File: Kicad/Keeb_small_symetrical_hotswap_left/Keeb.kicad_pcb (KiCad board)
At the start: 2 copper layers, 96.3 x 99.3 mm, 28 parts, among them J1 TYPE-C-31-M-12, SW1 CherryMX, SW10 CherryMX, SW11 CherryMX, SW13 CherryMX, SW14 CherryMX, SW15 CherryMX, SW16 CherryMX, SW17 CherryMX, SW18 CherryMX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

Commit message: added encoder
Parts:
- added U2: KY-040, KY-040:KY-040-PORT, F.Cu at (110.7, 38.4)
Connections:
- J1 pad A4_B9: 3v3 -> VSYS
- J1 pad B4_A9: 3v3 -> VSYS
- J1 pad B5: VSYS -> 3v3
- J1 pad B8: VSYS -> 3v3
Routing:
- net 3: track 0.00 -> 156.1 mm
- net 4: track 0.00 -> 153.3 mm
- net 3v3: track 171.4 -> 285.7 mm
- net 28: track 0.00 -> 111.4 mm
- net 0: track 147.0 -> 115.3 mm
- net GND: track 556.0 -> 525.5 mm
- net 1: track 120.3 -> 109.3 mm
- net VSYS: track 125.7 -> 116.3 mm
- net 2: track 115.6 -> 106.3 mm
- net 26: track 25.9 -> 23.0 mm
- net 18: track 48.2 -> 47.0 mm
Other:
- board size 96.3 x 99.3 mm -> 96.2 x 99.3 mm

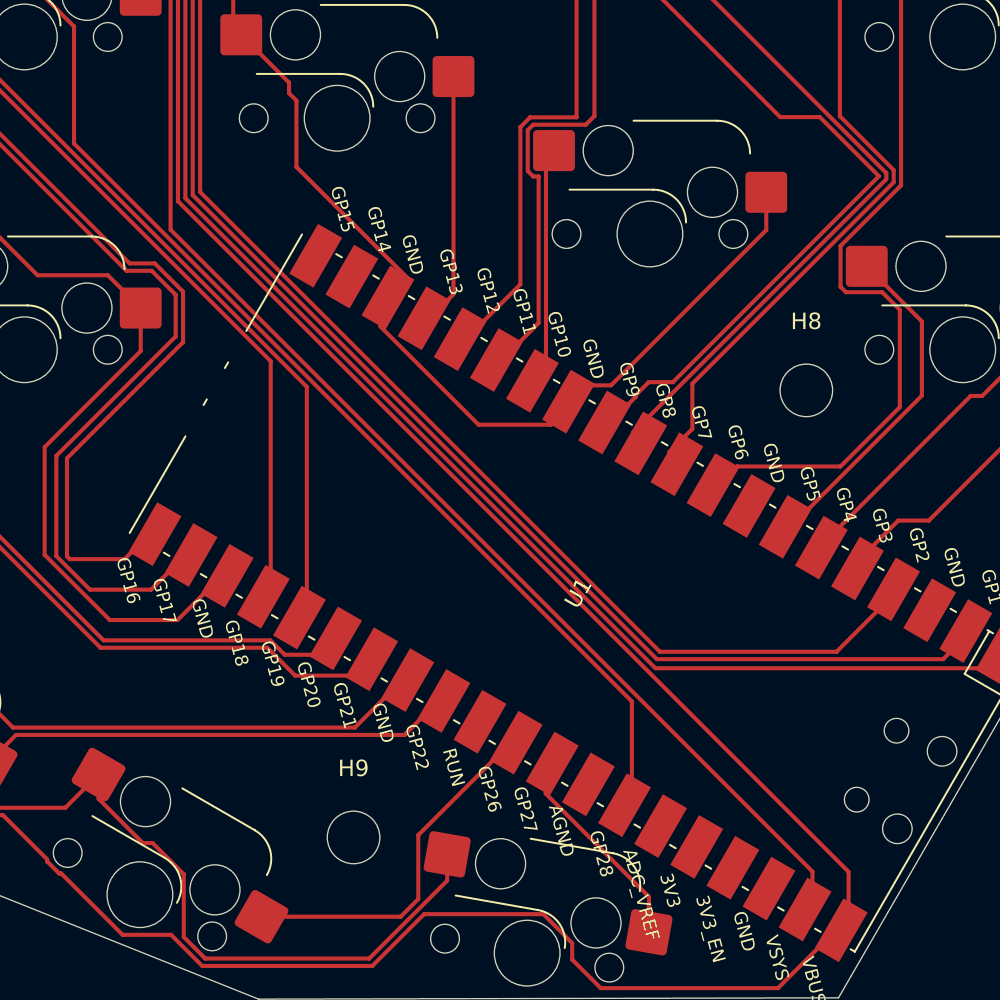
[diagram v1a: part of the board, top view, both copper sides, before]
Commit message: moved some traces
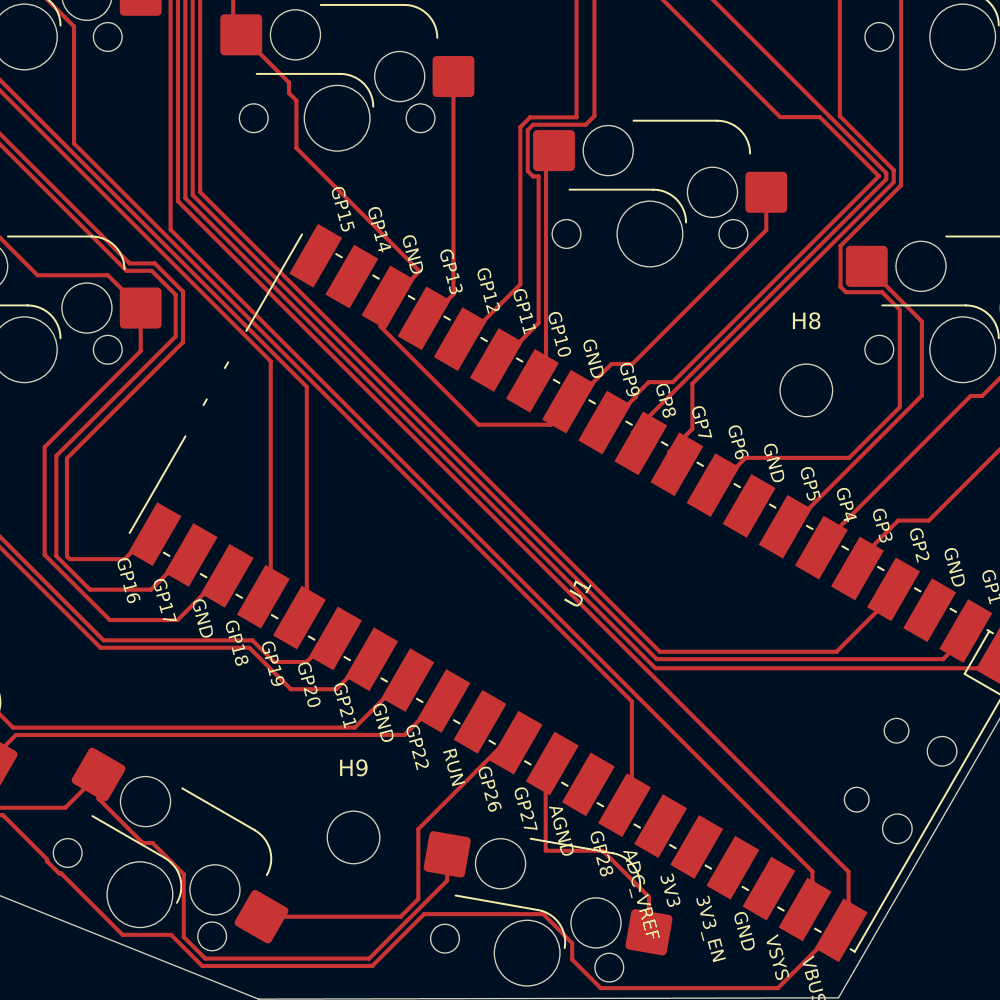
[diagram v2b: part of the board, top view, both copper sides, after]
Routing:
- net 27: track 14.0 -> 16.1 mm
- net 21: track 46.0 -> 46.7 mm

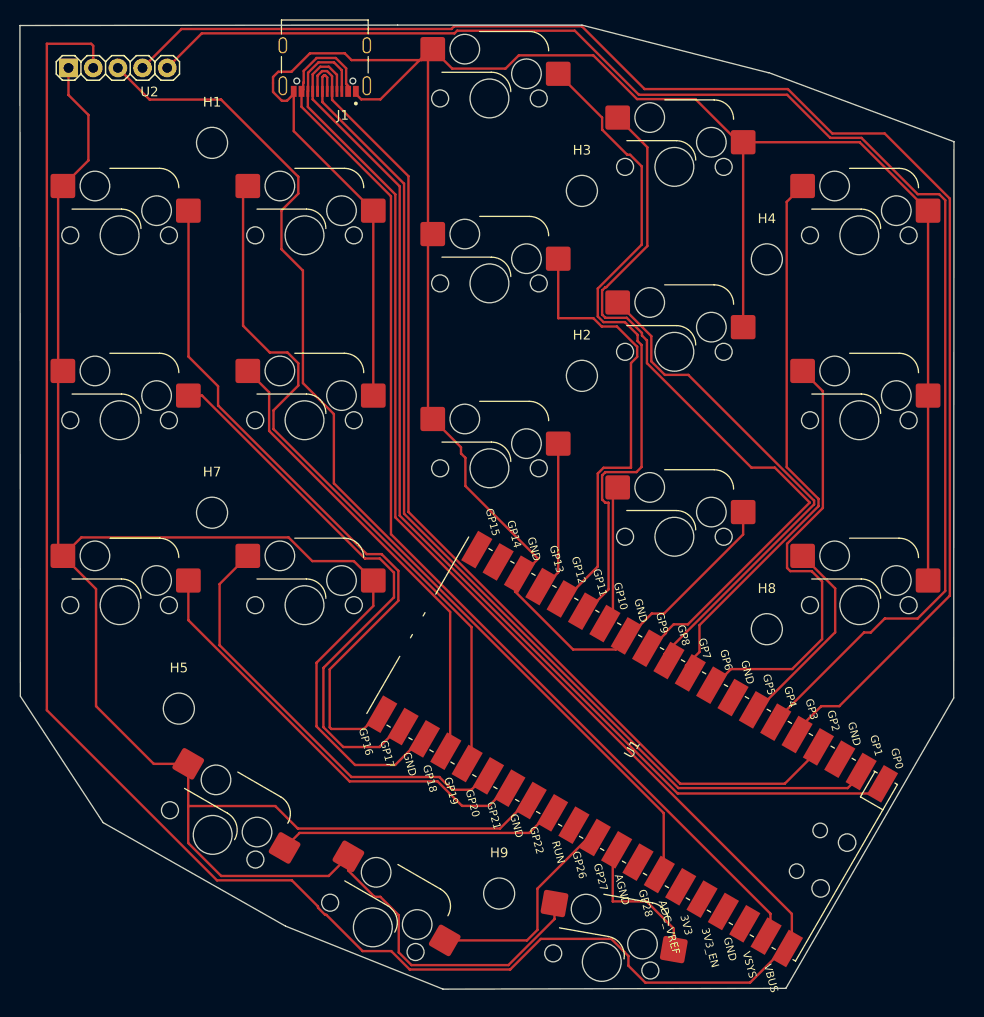
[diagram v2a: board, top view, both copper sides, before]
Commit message: Managed to add a button, optimised tracks, switched some connections around
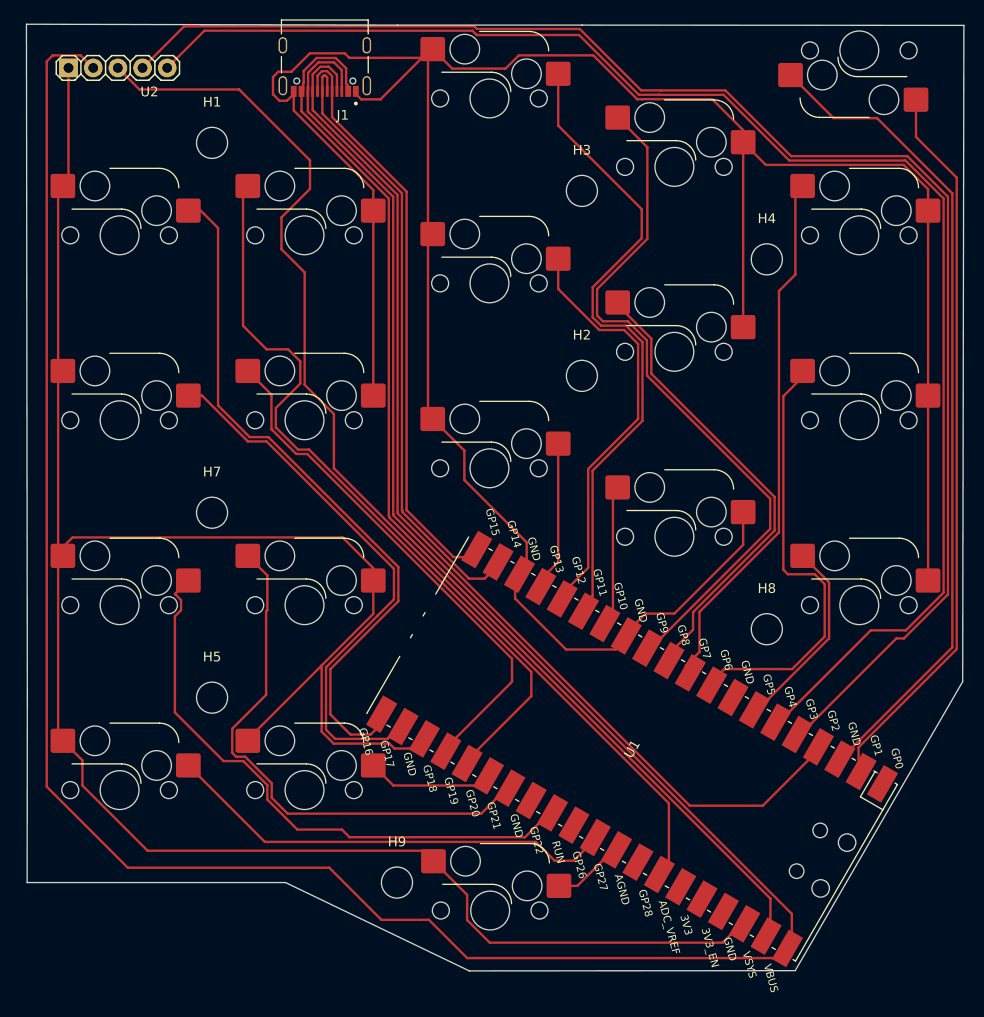
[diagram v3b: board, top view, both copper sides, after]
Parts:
- added SW2: CherryMX, ScottoKeebs_Hotswap:Hotswap_MX_1.00u, B.Cu at (188.3, 36.6)
- moved SW16 15.8 mm to (131.2, 112.8), turned to 180 degrees
- moved SW1 12.7 mm to (150.3, 125.2), turned to 180 degrees
- moved SW20 10.6 mm to (112.1, 112.8), turned to 180 degrees
- moved H9 10.6 mm to (140.7, 122.3)
- moved H5 3.60 mm to (121.7, 103.2)
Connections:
- J1 pad A5: 0 -> 2
- J1 pad A6: 1 -> 14
- J1 pad A7: 1 -> 14
- J1 pad A8: 0 -> 2
- J1 pad B6: 2 -> 15
- J1 pad B7: 2 -> 15
- SW15 pad 2: 20 -> 21
- SW16 pad 1: 26 -> 20
- SW19 pad 1: 21 -> 22
- SW20 pad 1: 22 -> 26
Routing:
- net 0: track 115.3 -> 0.00 mm
- net GND: track 526.0 -> 599.1 mm
- net 14: track 0.00 -> 63.0 mm
- net 15: track 0.00 -> 60.2 mm
- net 1: track 109.3 -> 76.0 mm
- net 20: track 45.6 -> 13.9 mm
- net 22: track 29.9 -> 61.6 mm
- net 26: track 23.2 -> 48.0 mm
- net 21: track 46.7 -> 56.5 mm
- net 27: track 16.1 -> 8.25 mm
- net 19: track 71.8 -> 77.8 mm
- net 18: track 47.0 -> 53.0 mm
- net 9: track 78.2 -> 73.2 mm
- net 2: track 106.3 -> 111.3 mm
- net 8: track 53.8 -> 49.1 mm
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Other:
- board size 96.2 x 99.3 mm -> 96.6 x 97.5 mm

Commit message: Worked a bit on the edge-cuts
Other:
- board size 96.6 x 97.5 mm -> 96.2 x 97.6 mm
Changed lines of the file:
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@@
     )
   )
-  (gr_poly
-    (pts
-      (xy 199.1 33.992944)
-      (xy 159.76 33.962944)
-      (xy 140.76 33.962944)
-      (xy 102.53 33.872944)
-      (xy 102.62 103.232944)
-      (xy 102.6 122.292944)
-      (xy 129.22 122.292944)
-      (xy 148.15 131.392944)
-      (xy 181.725 131.367944)
-      (xy 198.975 101.592944)
-    )
-    (stroke (width 0.05) (type solid)) (fill none) (layer "Edge.Cuts"))
+  (gr_line (start 102.6 37.520444) (end 102.6 118.482944)
+    (stroke (width 0.05) (type default)) (layer "Edge.Cuts"))
+  (gr_line (start 198.8025 102.290444) (end 198.8025 37.520444)
+    (stroke (width 0.05) (type default)) (layer "Edge.Cuts"))
+  (gr_line (start 148.32 131.341694) (end 182.13375 131.341694)
+    (stroke (width 0.05) (type default)) (layer "Edge.Cuts"))
+  (gr_arc (start 102.6 37.520444) (mid 103.715923 34.826367) (end 106.41 33.710444)
+    (stroke (width 0.05) (type default)) (layer "Edge.Cuts"))
+  (gr_line (start 194.9925 33.710444) (end 106.41 33.710444)
+    (stroke (width 0.05) (type default)) (layer "Edge.Cuts"))
+  (gr_line (start 129.27 122.292944) (end 148.32 131.341694)
+    (stroke (width 0.05) (type default)) (layer "Edge.Cuts"))
+  (gr_arc (start 194.9925 33.710444) (mid 197.686577 34.826367) (end 198.8025 37.520444)
+    (stroke (width 0.05) (type default)) (layer "Edge.Cuts"))
+  (gr_line (start 106.41 122.292944) (end 129.27 122.292944)
+    (stroke (width 0.05) (type default)) (layer "Edge.Cuts"))
+  (gr_arc (start 106.41 122.292944) (mid 103.715923 121.177021) (end 102.6 118.482944)
+    (stroke (width 0.05) (type default)) (layer "Edge.Cuts"))
+  (gr_line (start 182.13375 131.341694) (end 198.8025 102.290444)
+    (stroke (width 0.05) (type default)) (layer "Edge.Cuts"))
   (segment (start 179.15 82.75934) (end 179.15 85.848312) (width 0.25) (layer "F.Cu") (net 1))
   (segment (start 166.49 46.544944) (end 166.49 55.982944) (width 0.25) (layer "F.Cu") (net 1))
@@
   (segment (start 138.26 50.952944) (end 130.065 42.757944) (width 0.25) (layer "F.Cu") (net 15))
   (segment (start 135.095 86.737944) (end 107.285 86.737944) (width 0.25) (layer "F.Cu") (net 15))
-  (segment (start 104.62 112.412944) (end 112.97 120.762944) (width 0.25) (layer "F.Cu") (net 16))
   (segment (start 140.31 51.646448) (end 131.515 42.851448) (width 0.25) (layer "F.Cu") (net 16))
   (segment (start 140.34 84.482219) (end 140.34 84.32736) (width 0.25) (layer "F.Cu") (net 16))
-  (segment (start 133.72 120.762944) (end 139.09 126.132944) (width 0.25) (layer "F.Cu") (net 16))
+  (segment (start 105.755 36.567944) (end 104.62 37.702944) (width 0.25) (layer "F.Cu") (net 16))
   (segment (start 131.515 42.851448) (end 131.515 40.79) (width 0.25) (layer "F.Cu") (net 16))
   (segment (start 140.34 84.32736) (end 140.31 84.29736) (width 0.25) (layer "F.Cu") (net 16))
   (segment (start 135.015 38.605812) (end 135.015 40.79) (width 0.25) (layer "F.Cu") (net 16))
+  (segment (start 133.72 120.762944) (end 139.09 126.132944) (width 0.25) (layer "F.Cu") (net 16))
+  (segment (start 109.41 38.372944) (end 107.605 36.567944) (width 0.25) (layer "F.Cu") (net 16))
   (segment (start 131.54 38.870812) (end 132.610812 37.8) (width 0.25) (layer "F.Cu") (net 16))
-  (segment (start 104.62 37.702944) (end 104.62 112.412944) (width 0.25) (layer "F.Cu") (net 16))
-  (segment (start 143.99 126.132944) (end 147.930877 130.073821) (width 0.25) (layer "F.Cu") (net 16))
+  (segment (start 104.62 112.412944) (end 112.97 120.762944) (width 0.25) (layer "F.Cu") (net 16))
   (segment (start 131.515 40.79) (end 131.54 40.765) (width 0.25) (layer "F.Cu") (net 16))
-  (segment (start 140.31 84.29736) (end 140.31 51.646448) (width 0.25) (layer "F.Cu") (net 16))
   (segment (start 112.97 120.762944) (end 133.72 120.762944) (width 0.25) (layer "F.Cu") (net 16))
   (segment (start 139.09 126.132944) (end 143.99 126.132944) (width 0.25) (layer "F.Cu") (net 16))
+  (segment (start 140.31 84.29736) (end 140.31 51.646448) (width 0.25) (layer "F.Cu") (net 16))
+  (segment (start 143.99 126.132944) (end 147.930877 130.073821) (width 0.25) (layer "F.Cu") (net 16))
   (segment (start 181.37414 125.516359) (end 140.34 84.482219) (width 0.25) (layer "F.Cu") (net 16))
-  (segment (start 179.599173 130.073821) (end 181.37414 128.298854) (width 0.25) (layer "F.Cu") (net 16))
   (segment (start 181.37414 128.298854) (end 181.37414 125.516359) (width 0.25) (layer "F.Cu") (net 16))
-  (segment (start 109.41 38.372944) (end 108.1198 37.082744) (width 0.25) (layer "F.Cu") (net 16))
-  (segment (start 105.2402 37.082744) (end 104.62 37.702944) (width 0.25) (layer "F.Cu") (net 16))
+  (segment (start 104.62 37.702944) (end 104.62 112.412944) (width 0.25) (layer "F.Cu") (net 16))
   (segment (start 132.610812 37.8) (end 134.209188 37.8) (width 0.25) (layer "F.Cu") (net 16))
   (segment (start 134.209188 37.8) (end 135.015 38.605812) (width 0.25) (layer "F.Cu") (net 16))
+  (segment (start 107.605 36.567944) (end 105.755 36.567944) (width 0.25) (layer "F.Cu") (net 16))
+  (segment (start 131.54 40.765) (end 131.54 38.870812) (width 0.25) (layer "F.Cu") (net 16))
   (segment (start 147.930877 130.073821) (end 179.599173 130.073821) (width 0.25) (layer "F.Cu") (net 16))
-  (segment (start 131.54 40.765) (end 131.54 38.870812) (width 0.25) (layer "F.Cu") (net 16))
-  (segment (start 108.1198 37.082744) (end 105.2402 37.082744) (width 0.25) (layer "F.Cu") (net 16))
+  (segment (start 179.599173 130.073821) (end 181.37414 128.298854) (width 0.25) (layer "F.Cu") (net 16))
   (segment (start 188.064435 111.630922) (end 188.250853 111.444504) (width 0.25) (layer "F.Cu") (net 23))
   (segment (start 188.250853 108.356335) (end 198.36 98.247188) (width 0.25) (layer "F.Cu") (net 23))

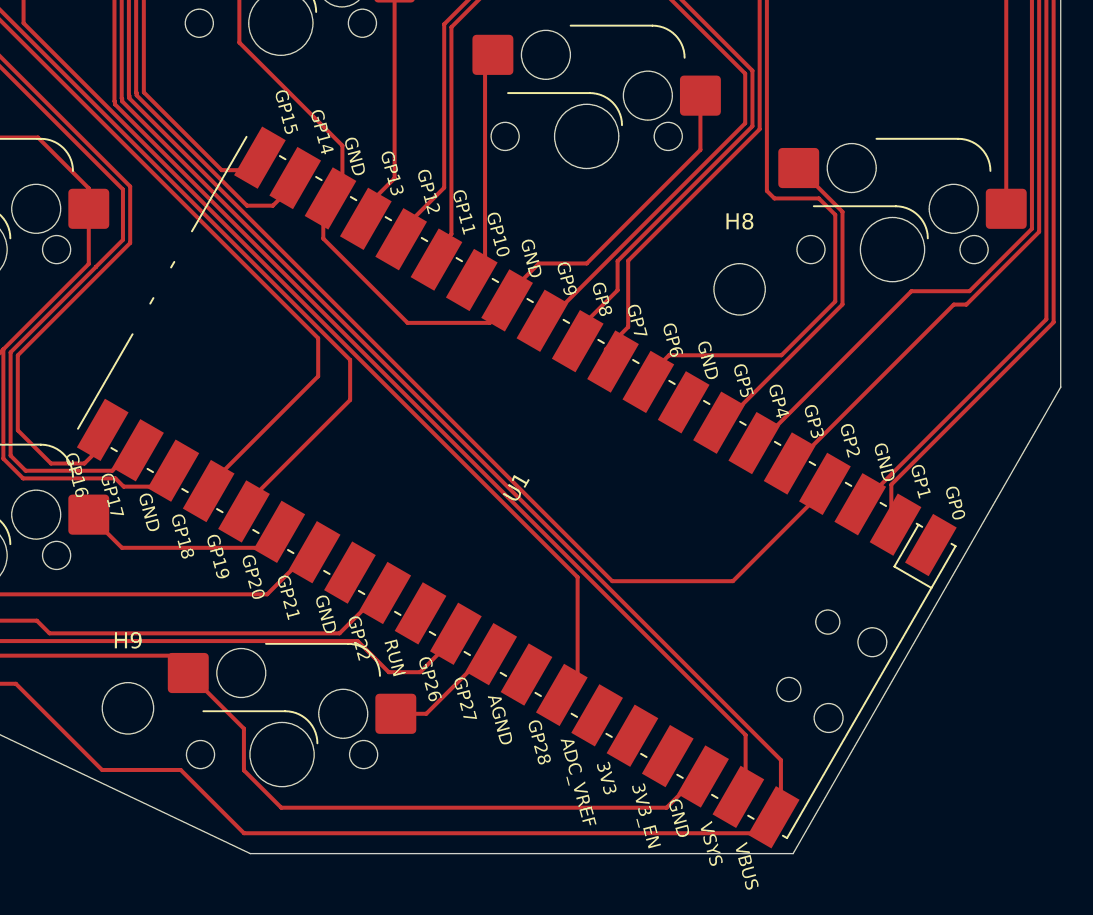
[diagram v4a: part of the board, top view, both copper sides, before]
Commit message: Updated a PiPico footprint
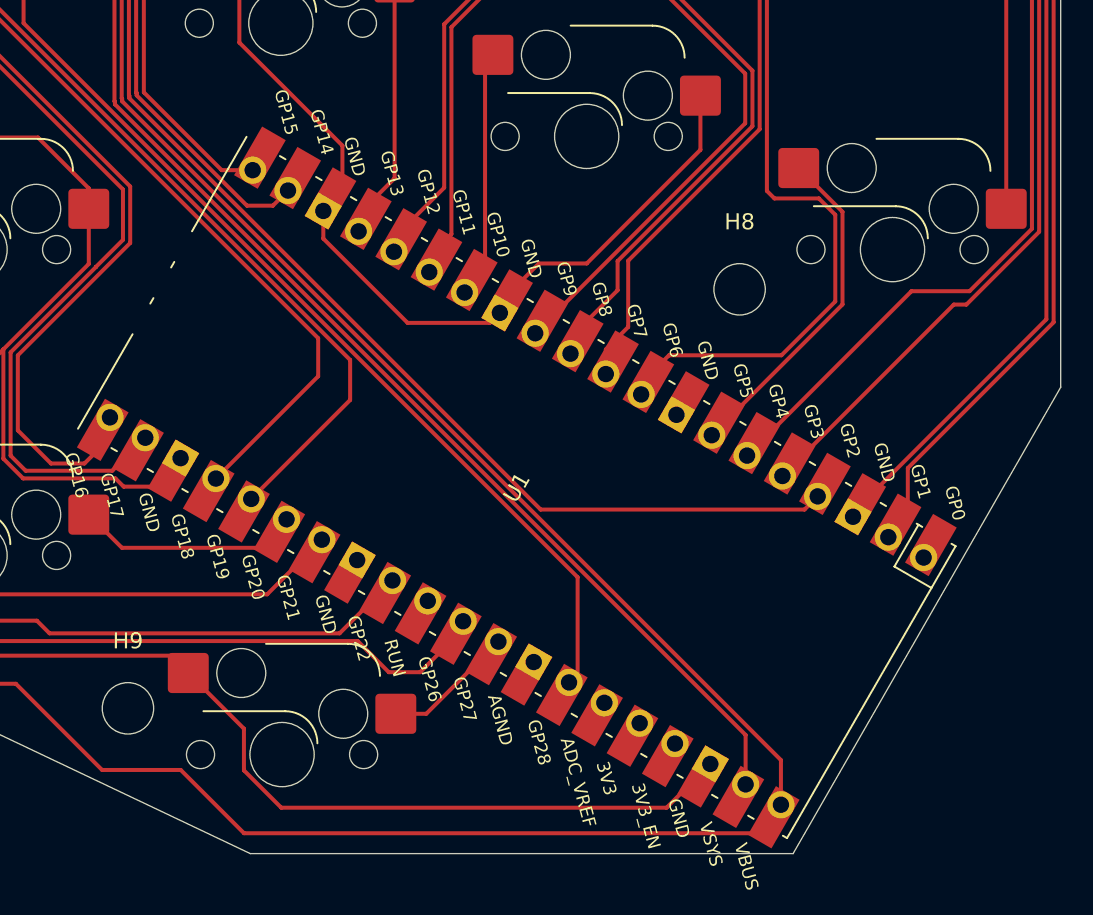
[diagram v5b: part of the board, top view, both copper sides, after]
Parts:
- U1: footprint MCU_RaspberryPi_and_Boards:RPi_Pico_SMD_TH_NO_HOLES -> MCU_RaspberryPi_and_Boards:RPi_Pico_SMD_TH_NO_BACK_HOLES
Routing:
- net 2: track 111.3 -> 107.6 mm
